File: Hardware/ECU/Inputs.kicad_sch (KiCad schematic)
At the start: 41 parts, among them J4 EBC05DRXN, SW5 SW_DPDT_x2, U11 KP234, U12 LMV324LIDT, U13 SP720

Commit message: modified:   .gitmodules 	modified:   Hardware/ECU/Comms.kicad_sch 	modified:   Hardware/ECU/ECU.kicad_pcb 	modified:   Hardware/ECU/ECU.kicad_pro 	modified:   Hardware/ECU/ECU.kicad_sch 	modified:   Hardware/ECU/Inputs.kicad_sch 	modified:   Hardware/ECU/Outputs.kicad_sch 	modified:   Hardware/ECU/fp-info-cache 	modified:   Hardware/ECU/fp-lib-table 	deleted:    docs/ECU info.url 	modified:   tune/Hayabusa-R1/CurrentTune.msq 	modified:   tune/Hayabusa-R1/projectCfg/project.properties 	modified:   tune/Hayabusa-R1/projectCfg/project.properties.bkup 	Hardware/ECU/ECU-backups/ECU-2024-11-07_084642.zip 	Hardware/ECU/ECU-backups/ECU-2024-11-07_091524.zip 	Hardware/ECU/ECU-backups/ECU-2024-11-07_094217.zip 	Hardware/ECU/ECU-backups/ECU-2024-11-07_120300.zip 	Hardware/ECU/ECU-backups/ECU-2024-11-08_085235.zip 	Hardware/ECU/ECU-backups/ECU-2024-11-08_091401.zip 	Hardware/ECU/ECU-backups/ECU-2024-11-08_103901.zip 	Hardware/ECU/docs/ 	Hardware/ECU/lib/2999/ 	Hardware/ECU/lib/IC_Automotive/IC_Automotive.pretty/BAT_2999.kicad_mod 	Hardware/ECU/lib/IC_Automotive/IC_Automotive.pretty/ZXMS6006DT8TA.kicad_mod 	Hardware/ECU/lib/ZXMS6006DT8TA/ 	Hardware/ECU/lib/teensy_library/ 	Hardware/ECU/output.pdf 	Hardware/ECU/report.txt 	docs/Speeduino_manual.pdf 	docs/Speeduino_manual.pdf:Zone.Identifier 	tune/Hayabusa-R1/dashboard/lambdaTable1Map.dash 	tune/Hayabusa-R1/dashboard/stagingMap.dash 	tune/TunerStudioAppDebug.txt
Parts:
- R28: footprint Resistor_SMD:R_0603_1608Metric_Pad1.05x0.95mm_HandSolder -> Resistor_SMD:R_0805_2012Metric_Pad1.20x1.40mm_HandSolder
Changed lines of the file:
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@@
 			)
 		)
-		(property "Footprint" "Resistor_SMD:R_0603_1608Metric_Pad1.05x0.95mm_HandSolder"
+		(property "Footprint" "Resistor_SMD:R_0805_2012Metric_Pad1.20x1.40mm_HandSolder"
 			(at 44.958 116.84 90)
 			(effects

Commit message: PCB
Platine Vernetzt
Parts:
- removed C19: 0.01uF, Capacitor_SMD:C_0805_2012Metric, symbol Device:C
- removed C22: 1uF, Capacitor_SMD:C_0805_2012Metric, symbol Device:C
- removed J4: EBC05DRXN, Misc:EBC05DRXN, symbol Misc:EBC05DRXN
- removed SW5: SW_DPDT_x2, Misc:AYZ0202AGRLC, symbol Misc:AYZ0202AGRLC
- removed U11: KP234, Misc:KP234, symbol Misc:KP234
- added C41: 0.1uF, Capacitor_SMD:C_0805_2012Metric, symbol Device:C
- added R70: 0, Resistor_SMD:R_0805_2012Metric, symbol Device:R
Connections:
- net GND: now also C41.1
- net MAP-5V: now also C41.2, R70.2
- net Baro_Sensor: now reaches R37.1
- new net Static_Air: R70.1
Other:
- note added: "Static Air"
- note removed: "MAP Sensor"
- moved on the sheet: C23, R37

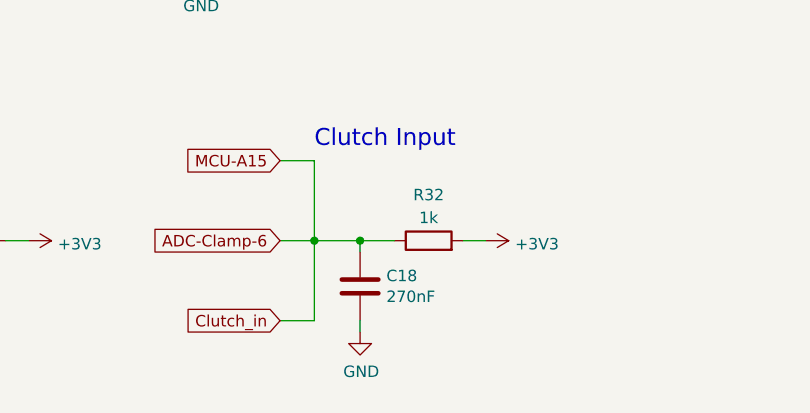
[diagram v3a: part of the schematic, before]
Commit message: PCB v0.2
leiterbahndicke updated
Clutch input rework
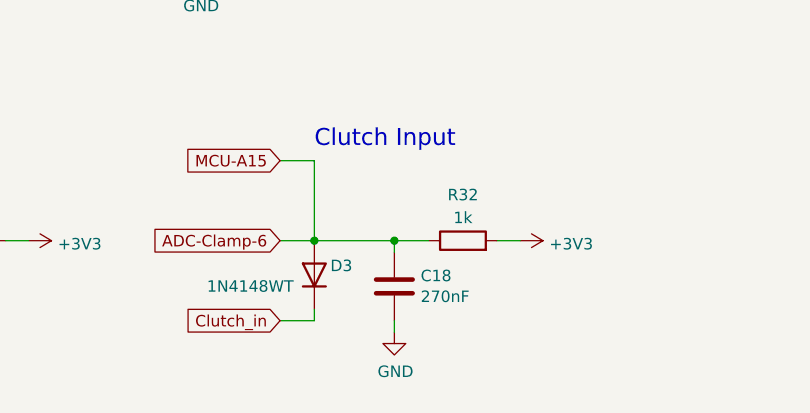
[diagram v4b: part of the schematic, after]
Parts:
- added D3: 1N4148WT, Diode_SMD:D_SOD-523, symbol Diode:1N4148WT
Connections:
- net ADC-Clamp-6: now also D3.2 (A)
- new net Clutch_in: D3.1 (K)
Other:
- moved on the sheet: C18, R32
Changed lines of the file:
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@@
 	)
 	(junction
-		(at 95.25 172.72)
+		(at 99.06 172.72)
 		(diameter 0)
 		(color 0 0 0 0)
@@
 	(wire
 		(pts
+			(xy 90.17 181.61) (xy 90.17 180.34)
+		)
+		(stroke
+			(width 0)
+			(type default)
+		)
+	)
+	(wire
+		(pts
 			(xy 241.3 36.83) (xy 237.49 36.83)
 		)
@@
 	(wire
 		(pts
+			(xy 86.36 181.61) (xy 90.17 181.61)
+		)
+		(stroke
+			(width 0)
+			(type default)
+		)
+	)
+	(wire
+		(pts
 			(xy 251.46 156.21) (xy 251.46 158.75)
 		)
@@
 	(wire
 		(pts
-			(xy 106.68 172.72) (xy 109.22 172.72)
+			(xy 110.49 172.72) (xy 113.03 172.72)
 		)
 		(stroke
@@
 	(wire
 		(pts
-			(xy 95.25 181.61) (xy 95.25 182.88)
+			(xy 99.06 181.61) (xy 99.06 182.88)
 		)
 		(stroke
@@
 	(wire
 		(pts
-			(xy 90.17 172.72) (xy 95.25 172.72)
+			(xy 90.17 172.72) (xy 99.06 172.72)
 		)
 		(stroke
@@
 	(wire
 		(pts
-			(xy 90.17 181.61) (xy 90.17 172.72)
-		)
-		(stroke
-			(width 0)
-			(type default)
-		)
-	)
-	(wire
-		(pts
 			(xy 45.72 172.72) (xy 40.64 172.72)
 		)
@@
 	(wire
 		(pts
-			(xy 86.36 181.61) (xy 90.17 181.61)
-		)
-		(stroke
-			(width 0)
-			(type default)
-		)
-	)
-	(wire
-		(pts
 			(xy 200.66 90.17) (xy 200.66 74.93)
 		)
@@
 	(wire
 		(pts
-			(xy 95.25 172.72) (xy 99.06 172.72)
+			(xy 99.06 172.72) (xy 102.87 172.72)
 		)
 		(stroke
@@
 	(wire
 		(pts
-			(xy 95.25 173.99) (xy 95.25 172.72)
+			(xy 99.06 173.99) (xy 99.06 172.72)
 		)
 		(stroke
@@
 	(symbol
 		(lib_id "power:+3V3")
-		(at 109.22 172.72 270)
+		(at 113.03 172.72 270)
 		(unit 1)
 		(exclude_from_sim no)
@@
 		(dnp no)
 		(property "Reference" "#PWR058"
-			(at 105.41 172.72 0)
+			(at 109.22 172.72 0)
 			(effects
 				(font
@@
 		)
 		(property "Value" "+3V3"
-			(at 112.4712 173.101 90)
+			(at 116.2812 173.101 90)
 			(effects
 				(font
@@
 		)
 		(property "Footprint" ""
-			(at 109.22 172.72 0)
+			(at 113.03 172.72 0)
 			(effects
 				(font
@@
 		)
 		(property "Datasheet" ""
-			(at 109.22 172.72 0)
+			(at 113.03 172.72 0)
 			(effects
 				(font
@@
 		)
 		(property "Description" ""
-			(at 109.22 172.72 0)
+			(at 113.03 172.72 0)
 			(effects
 				(font
@@
 	(symbol
 		(lib_id "power:GND")
-		(at 95.25 182.88 0)
+		(at 99.06 182.88 0)
 		(unit 1)
 		(exclude_from_sim no)
@@
 		(dnp no)
 		(property "Reference" "#PWR057"
-			(at 95.25 189.23 0)
+			(at 99.06 189.23 0)
 			(effects
 				(font
@@
 		)
 		(property "Value" "GND"
-			(at 95.377 187.2742 0)
+			(at 99.187 187.2742 0)
 			(effects
 				(font
@@
 		)
 		(property "Footprint" ""
-			(at 95.25 182.88 0)
+			(at 99.06 182.88 0)
 			(effects
 				(font
@@
 		)
 		(property "Datasheet" ""
-			(at 95.25 182.88 0)
+			(at 99.06 182.88 0)
 			(effects
 				(font
@@
 		)
 		(property "Description" ""
-			(at 95.25 182.88 0)
+			(at 99.06 182.88 0)
 			(effects
 				(font
@@
 	)
 	(symbol
+		(lib_id "Diode:1N4148WT")
+		(at 90.17 176.53 90)
+		(unit 1)
+		(exclude_from_sim no)
+		(in_bom yes)
+		(on_board yes)
+		(dnp no)
+		(property "Reference" "D3"
+			(at 91.948 175.514 90)
+			(effects
+				(font
+					(size 1.27 1.27)
+				)
+				(justify right)
+			)
+		)
+		(property "Value" "1N4148WT"
+			(at 78.232 177.8 90)
+			(effects
+				(font
+					(size 1.27 1.27)
+				)
+				(justify right)
+			)
+		)
+		(property "Footprint" "Diode_SMD:D_SOD-523"
+			(at 94.615 176.53 0)
+			(effects
+				(font
+					(size 1.27 1.27)
+				)
+				(hide yes)
+			)
+		)
+		(property "Datasheet" "https://www.diodes.com/assets/Datasheets/ds30396.pdf"
+			(at 90.17 176.53 0)
+			(effects
+				(font
+					(size 1.27 1.27)
+				)
+				(hide yes)
+			)
+		)
+		(property "Description" "75V 0.15A Fast switching Diode, SOD-523"
+			(at 90.17 176.53 0)
+			(effects
+				(font
+					(size 1.27 1.27)
+				)
+				(hide yes)
+			)
+		)
+		(property "Sim.Device" "D"
+			(at 90.17 176.53 0)
+			(effects
+				(font
+					(size 1.27 1.27)
+				)
+				(hide yes)
+			)
+		)
+		(property "Sim.Pins" "1=K 2=A"
+			(at 90.17 176.53 0)
+			(effects
+				(font
+					(size 1.27 1.27)
+				)
+				(hide yes)
+			)
+		)
+		(pin "2"
+		)
+		(pin "1"
+		)
+		(instances
+			(project ""
+				(path "/aaebd8f9-fdac-426b-87c0-a208167b6035/6dc40af5-f3aa-4e23-baf5-2c7690c42731"
+					(reference "D3")
+					(unit 1)
+				)
+			)
+		)
+	)
+	(symbol
 		(lib_id "Device:R")
-		(at 102.87 172.72 90)
+		(at 106.68 172.72 90)
 		(unit 1)
 		(exclude_from_sim no)
@@
 		(dnp no)
 		(property "Reference" "R32"
-			(at 102.87 167.64 90)
+			(at 106.68 167.64 90)
 			(effects
 				(font
@@
 		)
 		(property "Value" "1k"
-			(at 102.87 170.18 90)
+			(at 106.68 170.18 90)
 			(effects
 				(font
@@
 		)
 		(property "Footprint" "Resistor_SMD:R_0805_2012Metric"
-			(at 102.87 174.498 90)
+			(at 106.68 174.498 90)
 			(effects
 				(font
@@
 		)
 		(property "Datasheet" "~"
-			(at 102.87 172.72 0)
+			(at 106.68 172.72 0)
 			(effects
 				(font
@@
 		)
 		(property "Description" ""
-			(at 102.87 172.72 0)
+			(at 106.68 172.72 0)
 			(effects
 				(font
@@
 		)
 		(property "Digikey Part Number" "311-1.00KCRCT-ND"
-			(at 102.87 172.72 0)
+			(at 106.68 172.72 0)
 			(effects
 				(font
@@
 		)
 		(property "Manufacturer_Name" "Yageo"
-			(at 102.87 172.72 0)
+			(at 106.68 172.72 0)
 			(effects
 				(font
@@
 		)
 		(property "Manufacturer_Part_Number" "RC0805FR-071KL"
-			(at 102.87 172.72 0)
+			(at 106.68 172.72 0)
 			(effects
 				(font
@@
 		)
 		(property "URL" "https://www.digikey.com/product-detail/en/yageo/RC0805FR-071KL/311-1.00KCRCT-ND/730391"
-			(at 102.87 172.72 0)
+			(at 106.68 172.72 0)
 			(effects
 				(font
@@
 	(symbol
 		(lib_id "Device:C")
-		(at 95.25 177.8 0)
+		(at 99.06 177.8 0)
 		(unit 1)
 		(exclude_from_sim no)
@@
 		(dnp no)
 		(property "Reference" "C18"
-			(at 98.171 176.6316 0)
+			(at 101.981 176.6316 0)
 			(effects
 				(font
@@
 		)
 		(property "Value" "270nF"
-			(at 98.171 178.943 0)
+			(at 101.981 178.943 0)
 			(effects
 				(font
@@
 		)
 		(property "Footprint" "Capacitor_SMD:C_0805_2012Metric"
-			(at 96.2152 181.61 0)
+			(at 100.0252 181.61 0)
 			(effects
 				(font
@@
 		)
 		(property "Datasheet" "~"
-			(at 95.25 177.8 0)
+			(at 99.06 177.8 0)
 			(effects
 				(font
@@
 		)
 		(property "Description" ""
-			(at 95.25 177.8 0)
+			(at 99.06 177.8 0)
 			(effects
 				(font
@@
 		)
 		(property "Digikey Part Number" "311-4268-1-ND"
-			(at 95.25 177.8 0)
+			(at 99.06 177.8 0)
 			(effects
 				(font
@@
 		)
 		(property "Manufacturer_Name" "Yageo"
-			(at 95.25 177.8 0)
+			(at 99.06 177.8 0)
 			(effects
 				(font
@@
 		)
 		(property "Manufacturer_Part_Number" "CC0805JRX7R7BB274"
-			(at 95.25 177.8 0)
+			(at 99.06 177.8 0)
 			(effects
 				(font
@@
 		)
 		(property "URL" "https://www.digikey.com.au/product-detail/en/yageo/CC0805JRX7R7BB274/311-4268-1-ND/8025357"
-			(at 95.25 177.8 0)
+			(at 99.06 177.8 0)
 			(effects
 				(font

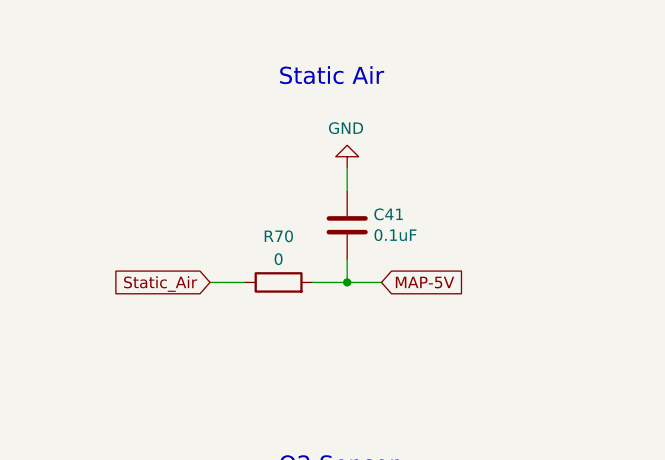
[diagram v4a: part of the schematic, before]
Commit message: modified:   Hardware/ECU/Conntectors.kicad_sch deleted:    Hardware/ECU/ECU-backups/ECU-2025-05-14_000421.zip deleted:    Hardware/ECU/ECU-backups/ECU-2025-05-14_001426.zip deleted:    Hardware/ECU/ECU-backups/ECU-2025-05-14_002531.zip deleted:    Hardware/ECU/ECU-backups/ECU-2025-05-14_003555.zip deleted:    Hardware/ECU/ECU-backups/ECU-2025-05-14_004055.zip modified:   Hardware/ECU/ECU.kicad_pcb modified:   Hardware/ECU/ECU.kicad_prl modified:   Hardware/ECU/ECU.kicad_pro modified:   Hardware/ECU/ECU.kicad_sch 	modified:   Hardware/ECU/Inputs.kicad_sch 	modified:   Hardware/ECU/Inputs2.kicad_sch 	modified:   Hardware/ECU/Schematics.pdf 	modified:   Hardware/ECU/docs/Pinout.ods 	Hardware/ECU/ECU-backups/ECU-2025-05-19_135220.zip 	Hardware/ECU/ECU-backups/ECU-2025-05-19_140656.zip 	Hardware/ECU/ECU-backups/ECU-2025-05-19_142320.zip 	Hardware/ECU/ECU-backups/ECU-2025-05-19_145225.zip 	Hardware/ECU/ECU-backups/ECU-2025-05-19_160311.zip 	Hardware/ECU/ECU.kicad_pcb.zip 	Hardware/ECU/docs/GPS.JPG 	docs/Kabelplan.pdn
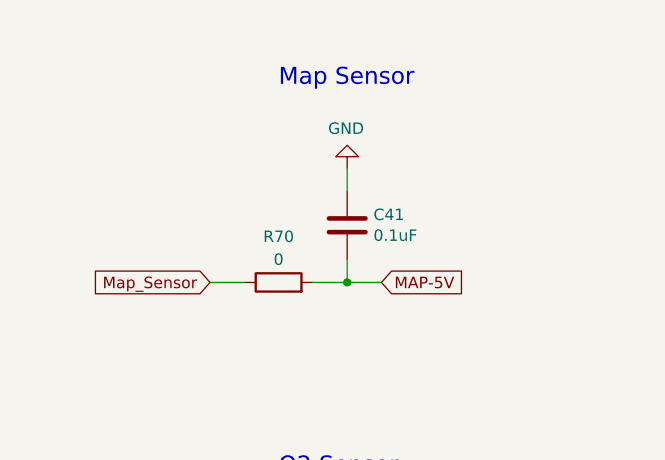
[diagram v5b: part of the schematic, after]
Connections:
- net Static_Air renamed Map_Sensor
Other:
- note added: "Map Sensor"
- note removed: "Static Air"
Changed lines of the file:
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@@
 		)
 	)
-	(text "Static Air"
+	(text "Map Sensor"
 		(exclude_from_sim no)
 		(at 46.99 21.59 0)
@@
 		)
 	)
-	(global_label "Static_Air"
+	(global_label "Map_Sensor"
 		(shape input)
 		(at 39.37 43.18 180)
@@
 		)
 		(property "Intersheetrefs" "${INTERSHEET_REFS}"
-			(at 27.4343 43.18 0)
-			(effects
-				(font
+			(at 25.2574 43.18 0)
+			(effects
+				(font

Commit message: deleted:    Hardware/ECU/ECU-backups/ECU-2025-05-27_235240.zip 	deleted:    Hardware/ECU/ECU-backups/ECU-2025-05-28_135321.zip 	deleted:    Hardware/ECU/ECU-backups/ECU-2025-05-28_140049.zip 	deleted:    Hardware/ECU/ECU-backups/ECU-2025-05-28_141416.zip 	deleted:    Hardware/ECU/ECU-backups/ECU-2025-05-28_154718.zip 	deleted:    Hardware/ECU/ECU-backups/ECU-2025-06-18_111329.zip 	new file:   Hardware/ECU/ECU-backups/ECU-2025-08-26_154141.zip 	new file:   Hardware/ECU/ECU-backups/ECU-2025-08-29_143817.zip 	new file:   Hardware/ECU/ECU-backups/ECU-2025-09-19_081818.zip 	new file:   Hardware/ECU/ECU-backups/ECU-2026-01-19_151411.zip 	new file:   Hardware/ECU/ECU-backups/ECU-2026-01-19_152057.zip 	new file:   Hardware/ECU/ECU-backups/ECU-2026-01-19_154705.zip 	modified:   Hardware/ECU/ECU.kicad_pcb 	modified:   Hardware/ECU/ECU.kicad_prl 	modified:   Hardware/ECU/ECU.kicad_sch 	modified:   Hardware/ECU/Inputs.kicad_sch 	modified:   Hardware/ECU/Inputs2.kicad_sch 	renamed:    Hardware/ECU/output/PCB.pdf -> Hardware/ECU/output/PCB-R9.3.pdf 	renamed:    Hardware/ECU/output/Schematics.pdf -> Hardware/ECU/output/Schematics-R0.3.pdf 	new file:   Hardware/ECU/output/Schematics-R1.pdf 	deleted:    Hardware/ECU/output/cut files/ECU-B_Cu.jpg 	modified:   speeduino (modified content)
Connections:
- net MCU-A0 renamed MCU-A4
- net MCU-A1 renamed MCU-A5
